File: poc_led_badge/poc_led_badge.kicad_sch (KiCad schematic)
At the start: 5 parts, among them SW1 SW_SPST

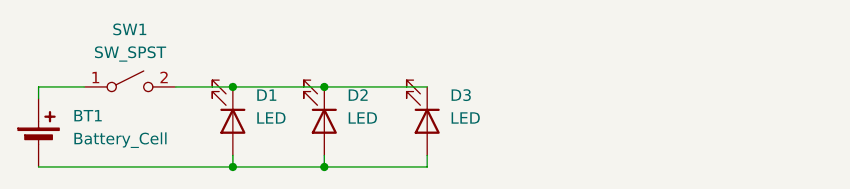
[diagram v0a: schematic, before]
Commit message: thicker traces, more leds
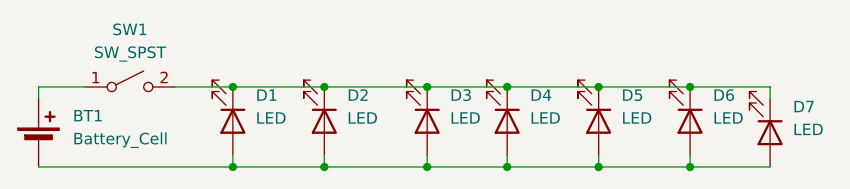
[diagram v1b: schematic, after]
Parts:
- added D4, D5, D6, D7: LED, Project footprints:LED_THT_SMD_Pads, symbol Device:LED
- D1, D2, D3: footprint LED_SMD:LED_THT_SMD_Pads -> Project footprints:LED_THT_SMD_Pads
- SW1: footprint Button_Switch_SMD:SW_Tactile_SPST_KAN-28 -> Project footprints:SW_Tactile_SPST_KAN-28
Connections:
- net at D1.1 (K), D2.1 (K), D3.1 (K)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: now also D4.1 (K), D5.1 (K), D6.1 (K), D7.1 (K)
- net at BT1.2 (-), D1.2 (A), D2.2 (A)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: now also D4.2 (A), D5.2 (A), D6.2 (A), D7.2 (A)
